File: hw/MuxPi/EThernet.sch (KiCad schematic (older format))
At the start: 36 parts, among them J3 TJACKCFL8P8CSR06M1, U11 93AA56AT-I/OT, U12 LAN9500A-ABZJ, Y3 25.00M-SMDHC49S

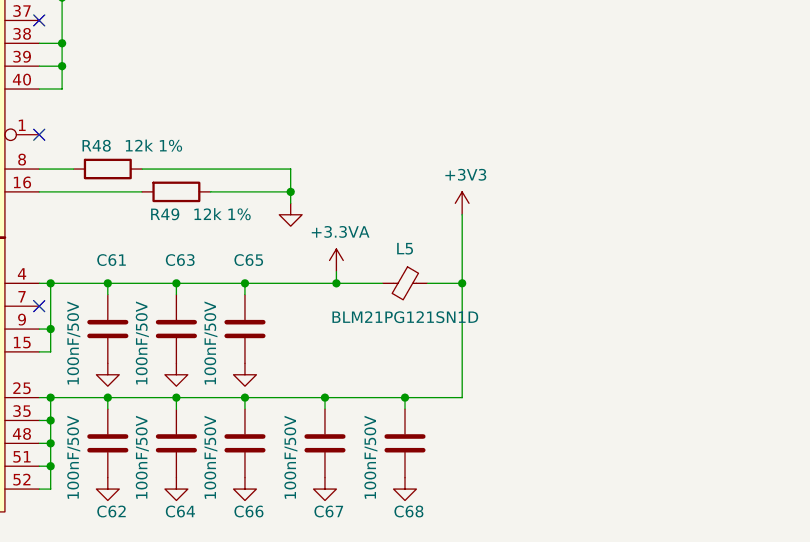
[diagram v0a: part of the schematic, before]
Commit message: Add detailed info to MuxPi electronic components
The additional information includes manufacturer names and
manufacturer symbols for all components except ceramic capacitors
and resistors. It allows to create BOM (Bill Of Materials) with
actual product names.

Change-Id: Id1c518bba60322d4b8b132ad14261806070abc27
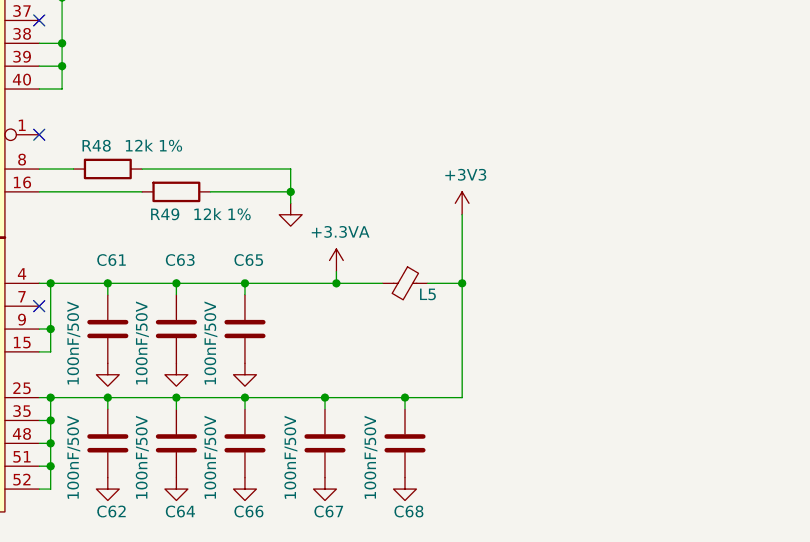
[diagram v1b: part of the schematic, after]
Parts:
- J3: Manufacturer (none) -> CZT; Symbol (none) -> JDFD10141104 TS-10014-11(6U)
- L3, L4, L5: Manufacturer (none) -> MURATA; Symbol (none) -> BLM21PG121SN1D
- U11: Manufacturer (none) -> MICROCHIP; Symbol (none) -> 93AA56AT-I/OT
- U12: Manufacturer (none) -> MICROCHIP; Symbol (none) -> LAN9500A-ABZJ
- Y3: Manufacturer (none) -> YIC; Symbol (none) -> 25.00M-SMDHC49S
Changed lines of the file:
@@
 F 3 "http://www.farnell.com/datasheets/1907741.pdf?_ga=1.91944537.291132730.1474618953" H 6150 2250 50  0001 C CNN
 F 4 "http://pl.farnell.com/microchip/lan9500a-abzj/ic-usb2-0-10-100-enet-cntrl-56vqfn/dp/2292585" H 4200 2500 60  0001 C CNN "Shop link"
+F 5 "LAN9500A-ABZJ" H 4200 2500 50  0001 C CNN "Symbol"
+F 6 "MICROCHIP" H 4200 2500 50  0001 C CNN "Manufacturer"
 	1    4200 2500
 	1    0    0    -1
@@
 F 3 "http://www.farnell.com/datasheets/1907741.pdf?_ga=1.91944537.291132730.1474618953" H 5800 6000 50  0001 C CNN
 F 4 "http://pl.farnell.com/microchip/lan9500a-abzj/ic-usb2-0-10-100-enet-cntrl-56vqfn/dp/2292585" H 3850 6250 60  0001 C CNN "Shop link"
+F 5 "MICROCHIP" H 3850 6250 50  0001 C CNN "Manufacturer"
+F 6 "LAN9500A-ABZJ" H 3850 6250 50  0001 C CNN "Symbol"
 	2    3850 6250
 	1    0    0    -1
@@
 $EndComp
 $Comp
-L MuxPi:Ferrite_Bead_Small L5
-U 1 1 585E1E42
-P 6250 6450
-F 0 "L5" V 6100 6450 50  0000 C CNN
-F 1 "BLM21PG121SN1D" V 6400 6450 50  0000 C CNN
-F 2 "Resistors_SMD:R_0805_HandSoldering" H 6350 6359 50  0001 L CNN
-F 3 "http://www.tme.eu/pl/Document/6052c7f9d4f1672121538e0d10f79ff8/blm21pg300sn1d.pdf" H 6350 6359 50  0001 L CNN
-F 4 "http://www.tme.eu/pl/details/blm21pg121sn1d/ferryty-koraliki/murata/" H 6250 6450 60  0001 C CNN "Shop link"
-	1    6250 6450
-	0    1    1    0
-$EndComp
-$Comp
 L MuxPi:GND #PWR0171
 U 1 1 585E2006
@@
 $EndComp
 $Comp
-L MuxPi:Ferrite_Bead_Small L4
-U 1 1 585E3856
-P 2450 6550
-F 0 "L4" V 2500 6650 50  0000 C CNN
-F 1 "BLM21PG121SN1D" V 2304 6550 50  0001 C CNN
-F 2 "Resistors_SMD:R_0805_HandSoldering" H 2550 6459 50  0001 L CNN
-F 3 "http://www.tme.eu/pl/Document/6052c7f9d4f1672121538e0d10f79ff8/blm21pg300sn1d.pdf" H 2550 6459 50  0001 L CNN
-F 4 "http://www.tme.eu/pl/details/blm21pg121sn1d/ferryty-koraliki/murata/" H 2450 6550 60  0001 C CNN "Shop link"
-	1    2450 6550
-	0    1    1    0
-$EndComp
-$Comp
 L MuxPi:GND #PWR0165
 U 1 1 585E3BDA
@@
 F 3 "http://www.tme.eu/pl/Document/6052c7f9d4f1672121538e0d10f79ff8/blm21pg300sn1d.pdf" H 2100 6359 50  0001 L CNN
 F 4 "http://www.tme.eu/pl/details/blm21pg121sn1d/ferryty-koraliki/murata/" H 2000 6450 60  0001 C CNN "Shop link"
+F 5 "MURATA" V 2000 6450 50  0001 C CNN "Manufacturer"
+F 6 "BLM21PG121SN1D" V 2000 6450 50  0001 C CNN "Symbol"
 	1    2000 6450
 	0    1    1    0
@@
 F 3 "http://www.tme.eu/pl/Document/6527d4ac6cd20f858e4312ccc80ef7ce/YIC-49US_49SMT-quartz_crystal.pdf" H 1900 6100 50  0001 C CNN
 F 4 "http://www.tme.eu/pl/details/25.00m-smdhc49s/rezonatory-kwarcowe-smd/yic/" V 1900 6100 60  0001 C CNN "Shop link"
+F 5 "YIC" V 1900 6100 50  0001 C CNN "Manufacturer"
+F 6 "25.00M-SMDHC49S" V 1900 6100 50  0001 C CNN "Symbol"
 	1    1900 6100
 	0    1    1    0
@@
 F 3 "http://www.farnell.com/datasheets/1669363.pdf?_ga=1.23852537.291132730.1474618953" H 2350 2600 50  0001 C CNN
 F 4 "http://pl.farnell.com/microchip/93aa56at-i-ot/serial-eeprom-2kbit-2mhz-sot-23/dp/1331419" H 2450 2600 60  0001 C CNN "Shop link"
+F 5 "MICROCHIP" H 2450 2600 50  0001 C CNN "Manufacturer"
+F 6 "93AA56AT-I/OT" H 2450 2600 50  0001 C CNN "Symbol"
 	1    2450 2600
 	-1   0    0    -1
@@
 F 3 "https://www.maritex.com.pl/product/attachment/41725/TJACKCFL8P8CSB06-MAG1_new.pdf" H 9050 2523 50  0001 C CNN
 F 4 "https://www.maritex.com.pl/zlacza/zlacza_rj_modularne/zlacza_rj_1_x_port/zlacza_rj_gniazda_modularne_ekranowane_diody_led_transformator_separujacy/tjackcfl8p8csr06m1.html" H 9300 1900 60  0001 C CNN "Shop link"
+F 5 "CZT" H 9300 1900 50  0001 C CNN "Manufacturer"
+F 6 "JDFD10141104 TS-10014-11(6U)" H 9300 1900 50  0001 C CNN "Symbol"
 	1    9300 1900
 	1    0    0    -1
@@
 Wire Wire Line
 	9950 2650 10100 2650
+$Comp
+L MuxPi:Ferrite_Bead_Small L4
+U 1 1 5A8E75C9
+P 2450 6550
+F 0 "L4" V 2500 6650 50  0000 C CNN
+F 1 "BLM21PG121SN1D" V 2304 6550 50  0001 C CNN
+F 2 "Resistors_SMD:R_0805_HandSoldering" H 2550 6459 50  0001 L CNN
+F 3 "http://www.tme.eu/pl/Document/6052c7f9d4f1672121538e0d10f79ff8/blm21pg300sn1d.pdf" H 2550 6459 50  0001 L CNN
+F 4 "http://www.tme.eu/pl/details/blm21pg121sn1d/ferryty-koraliki/murata/" H 2450 6550 60  0001 C CNN "Shop link"
+F 5 "MURATA" V 2450 6550 50  0001 C CNN "Manufacturer"
+F 6 "BLM21PG121SN1D" V 2450 6550 50  0001 C CNN "Symbol"
+	1    2450 6550
+	0    1    1    0
+$EndComp
+$Comp
+L MuxPi:Ferrite_Bead_Small L5
+U 1 1 5A8E7FF7
+P 6250 6450
+F 0 "L5" V 6300 6550 50  0000 C CNN
+F 1 "BLM21PG121SN1D" V 6104 6450 50  0001 C CNN
+F 2 "Resistors_SMD:R_0805_HandSoldering" H 6350 6359 50  0001 L CNN
+F 3 "http://www.tme.eu/pl/Document/6052c7f9d4f1672121538e0d10f79ff8/blm21pg300sn1d.pdf" H 6350 6359 50  0001 L CNN
+F 4 "http://www.tme.eu/pl/details/blm21pg121sn1d/ferryty-koraliki/murata/" H 6250 6450 60  0001 C CNN "Shop link"
+F 5 "MURATA" V 6250 6450 50  0001 C CNN "Manufacturer"
+F 6 "BLM21PG121SN1D" V 6250 6450 50  0001 C CNN "Symbol"
+	1    6250 6450
+	0    1    1    0
+$EndComp
 $EndSCHEMATC

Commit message: Update hardware design to version 1.3
Change-Id: I17b3f32943a6fd048f05d1b0d8676607dc54b976
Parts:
- C58, C59: footprint Capacitors_SMD:C_0402 -> Capacitors_SMD:C_0805
- L3, L4, L5: footprint Resistors_SMD:R_0805_HandSoldering -> Resistors_SMD:R_0805
- R48, R49: footprint Resistors_SMD:R_0402 -> Resistors_SMD:R_0805
- R56: value 330R -> 10K; Shop link http://www.tme.eu/pl/details/rc0805jr-07330r/rezystory-smd-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 -> (none)
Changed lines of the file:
@@
 Sheet 11 12
 Title "MuxPi"
-Date "2018-04-20"
-Rev "1.2"
+Date "2018-08-14"
+Rev "1.3"
 Comp "SRPOL"
 Comment1 "Author: Adam Malinowski <a.malinowsk2@partner.samsung.com>"
-Comment2 "Copyright (c) 2016 - 2018 Samsung Electronics Co., Ltd All Rights Reserved"
+Comment2 "Copyright (c) 2016 -2018 Samsung Electronics Co., Ltd All Rights Reserved"
 Comment3 ""
 Comment4 ""
@@
 F 0 "L3" V 2050 6550 50  0000 C CNN
 F 1 "BLM21PG121SN1D" V 1854 6450 50  0001 C CNN
-F 2 "Resistors_SMD:R_0805_HandSoldering" H 2100 6359 50  0001 L CNN
+F 2 "Resistors_SMD:R_0805" H 2100 6359 50  0001 L CNN
 F 3 "http://www.tme.eu/pl/Document/6052c7f9d4f1672121538e0d10f79ff8/blm21pg300sn1d.pdf" H 2100 6359 50  0001 L CNN
 F 4 "http://www.tme.eu/pl/details/blm21pg121sn1d/ferryty-koraliki/murata/" H 2000 6450 60  0001 C CNN "Shop link"
@@
 F 0 "C59" H 2350 5550 50  0000 L CNN
 F 1 "100nF/50V" H 2300 5050 50  0000 L CNN
-F 2 "Capacitors_SMD:C_0402" H 2538 5250 50  0001 C CNN
+F 2 "Capacitors_SMD:C_0805" H 2538 5250 50  0001 C CNN
 F 3 "http://www.tme.eu/pl/Document/4a42202b32dab16128fe107dd69598cc/samsung-chip-cap.pdf" H 2500 5400 50  0001 C CNN
 F 4 "http://www.tme.eu/pl/details/cl21b331kbannnc/kondensatory-mlcc-smd-0805/samsung/" H 2500 5400 60  0001 C CNN "Shop link"
@@
 F 0 "C58" H 2300 7200 50  0000 L CNN
 F 1 "100nF/50V" H 2050 6650 50  0000 L CNN
-F 2 "Capacitors_SMD:C_0402" H 2288 6900 50  0001 C CNN
+F 2 "Capacitors_SMD:C_0805" H 2288 6900 50  0001 C CNN
 F 3 "http://www.tme.eu/pl/Document/4a42202b32dab16128fe107dd69598cc/samsung-chip-cap.pdf" H 2250 7050 50  0001 C CNN
 F 4 "http://www.tme.eu/pl/details/cl21b331kbannnc/kondensatory-mlcc-smd-0805/samsung/" H 2250 7050 60  0001 C CNN "Shop link"
@@
 F 0 "R48" V 4850 5900 50  0000 C CNN
 F 1 "12k 1%" V 4850 6150 50  0000 C CNN
-F 2 "Resistors_SMD:R_0402" V 4880 5950 30  0001 C CNN
+F 2 "Resistors_SMD:R_0805" V 4880 5950 30  0001 C CNN
 F 3 "http://www.tme.eu/pl/Document/7b8fed8c112f8a94930279c22c957f7f/rc0805yageo.pdf" H 4950 5950 30  0001 C CNN
 F 4 "http://www.tme.eu/pl/details/rc0805fr-0712k/rezystory-smd-0805/yageo/rc0805fr-0712kl/" V 4950 5950 60  0001 C CNN "Shop link"
@@
 F 0 "R49" V 5350 6000 50  0000 C CNN
 F 1 "12k 1%" V 5350 6250 50  0000 C CNN
-F 2 "Resistors_SMD:R_0402" V 5180 6050 30  0001 C CNN
+F 2 "Resistors_SMD:R_0805" V 5180 6050 30  0001 C CNN
 F 3 "http://www.tme.eu/pl/Document/7b8fed8c112f8a94930279c22c957f7f/rc0805yageo.pdf" H 5250 6050 30  0001 C CNN
 F 4 "http://www.tme.eu/pl/details/rc0805fr-0712k/rezystory-smd-0805/yageo/rc0805fr-0712kl/" V 5250 6050 60  0001 C CNN "Shop link"
@@
 P 9800 2850
 F 0 "R56" H 9600 2900 50  0000 L CNN
-F 1 "330R" H 9500 2800 50  0000 L CNN
+F 1 "10K" H 9500 2800 50  0000 L CNN
 F 2 "Resistors_SMD:R_0805" V 9730 2850 50  0001 C CNN
 F 3 "http://www.tme.eu/pl/Document/7b8fed8c112f8a94930279c22c957f7f/rc0805yageo.pdf" H 9800 2850 50  0001 C CNN
-F 4 "http://www.tme.eu/pl/details/rc0805jr-07330r/rezystory-smd-0805/yageo/rc0805jr-07330rl/" V 9800 2850 60  0001 C CNN "Shop link"
 	1    9800 2850
 	1    0    0    -1
@@
 F 0 "L4" V 2500 6650 50  0000 C CNN
 F 1 "BLM21PG121SN1D" V 2304 6550 50  0001 C CNN
-F 2 "Resistors_SMD:R_0805_HandSoldering" H 2550 6459 50  0001 L CNN
+F 2 "Resistors_SMD:R_0805" H 2550 6459 50  0001 L CNN
 F 3 "http://www.tme.eu/pl/Document/6052c7f9d4f1672121538e0d10f79ff8/blm21pg300sn1d.pdf" H 2550 6459 50  0001 L CNN
 F 4 "http://www.tme.eu/pl/details/blm21pg121sn1d/ferryty-koraliki/murata/" H 2450 6550 60  0001 C CNN "Shop link"
@@
 F 0 "L5" V 6300 6550 50  0000 C CNN
 F 1 "BLM21PG121SN1D" V 6104 6450 50  0001 C CNN
-F 2 "Resistors_SMD:R_0805_HandSoldering" H 6350 6359 50  0001 L CNN
+F 2 "Resistors_SMD:R_0805" H 6350 6359 50  0001 L CNN
 F 3 "http://www.tme.eu/pl/Document/6052c7f9d4f1672121538e0d10f79ff8/blm21pg300sn1d.pdf" H 6350 6359 50  0001 L CNN
 F 4 "http://www.tme.eu/pl/details/blm21pg121sn1d/ferryty-koraliki/murata/" H 6250 6450 60  0001 C CNN "Shop link"

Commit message: Update  hardware design to version 1.4
Change-Id: I72a4381d8bec5616bc1cfe04dc8a5407141c77d5
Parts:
- removed Y3: 25.00M-SMDHC49S, Crystals:Q_49U3HMS, symbol MuxPi:Crystal
- added Y3: 25.00M-CFPX218, Crystal:Crystal_SMD_2520-4Pin_2.5x2.0mm, symbol Device:Crystal_GND24
- C54: value 30pF/50V -> 33pF/50V; Shop link http://www.tme.eu/pl/details/cl21c330jbannnd/kondensatory-m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 -> https://pl.farnell.com/walsin/0805n330j500ct/cap-33pf-50v-5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
- C55: value 30pF/50V -> 33pF/50V; footprint Capacitors_SMD:C_0805 -> MuxPi:C_0805; Shop link http://www.tme.eu/pl/details/cl21c330jbannnd/kondensatory-m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 -> https://pl.farnell.com/walsin/0805n330j500ct/cap-33pf-50v-5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
- R53, R54: value 330R -> 560R; Shop link http://www.tme.eu/pl/details/rc0805jr-07330r/rezystory-smd-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 -> https://www.tme.eu/pl/details/rc0805jr-07560r/rezystory-smd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
- U11: Assembly (none) -> DNP
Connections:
- net GND: now also Y3.2, Y3.4
- net at C55.1, U12.19 (XO): now also Y3.3
- net at C54.1, U12.18 (XI): now also Y3.1
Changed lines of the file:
@@
 EESchema Schematic File Version 4
 LIBS:MuxPi-cache
-EELAYER 26 0
+EELAYER 29 0
 EELAYER END
 $Descr A4 11693 8268
@@
 Sheet 11 12
 Title "MuxPi"
-Date "2018-08-14"
-Rev "1.3"
+Date "2018-11-16"
+Rev "1.4"
 Comp "SRPOL"
 Comment1 "Author: Adam Malinowski <a.malinowsk2@partner.samsung.com>"
@@
 $EndComp
 $Comp
-L MuxPi:Crystal Y3
-U 1 1 585EE4AB
-P 1900 6100
-F 0 "Y3" V 1750 6000 50  0000 C CNN
-F 1 "25.00M-SMDHC49S" V 1600 6100 50  0000 C CNN
-F 2 "Crystals:Q_49U3HMS" H 1900 6100 50  0001 C CNN
-F 3 "http://www.tme.eu/pl/Document/6527d4ac6cd20f858e4312ccc80ef7ce/YIC-49US_49SMT-quartz_crystal.pdf" H 1900 6100 50  0001 C CNN
-F 4 "http://www.tme.eu/pl/details/25.00m-smdhc49s/rezonatory-kwarcowe-smd/yic/" V 1900 6100 60  0001 C CNN "Shop link"
-F 5 "YIC" V 1900 6100 50  0001 C CNN "Manufacturer"
-F 6 "25.00M-SMDHC49S" V 1900 6100 50  0001 C CNN "Symbol"
-	1    1900 6100
-	0    1    1    0
-$EndComp
-$Comp
 L MuxPi:GND #PWR0156
 U 1 1 585EE4B2
@@
 P 1450 5850
 F 0 "C54" V 1300 5800 50  0000 L CNN
-F 1 "30pF/50V" V 1600 5700 50  0000 L CNN
+F 1 "33pF/50V" V 1600 5700 50  0000 L CNN
 F 2 "Capacitors_SMD:C_0805" H 1488 5700 30  0001 C CNN
-F 3 "http://www.tme.eu/pl/Document/4a42202b32dab16128fe107dd69598cc/samsung-chip-cap.pdf" H 1450 5850 60  0001 C CNN
-F 4 "http://www.tme.eu/pl/details/cl21c330jbannnd/kondensatory-mlcc-smd-0805/samsung/" V 1450 5850 60  0001 C CNN "Shop link"
+F 3 "http://www.farnell.com/datasheets/2340522.pdf" H 1450 5850 60  0001 C CNN
+F 4 "https://pl.farnell.com/walsin/0805n330j500ct/cap-33pf-50v-5-c0g-np0-0805-reel/dp/2495530" V 1450 5850 60  0001 C CNN "Shop link"
 	1    1450 5850
 	0    1    1    0
@@
 F 5 "MICROCHIP" H 2450 2600 50  0001 C CNN "Manufacturer"
 F 6 "93AA56AT-I/OT" H 2450 2600 50  0001 C CNN "Symbol"
+F 7 "DNP" H 2450 2300 50  0000 C CIB "Assembly"
 	1    2450 2600
 	-1   0    0    -1
@@
 	2200 6150 2200 6350
 Wire Wire Line
-	1200 5850 1200 6350
+	1200 5850 1200 6100
 Connection ~ 1200 6350
 Wire Wire Line
@@
 P 7100 2100
 F 0 "R53" V 7000 2050 50  0000 L CNN
-F 1 "330R" V 7050 2250 50  0000 L CNN
+F 1 "560R" V 7050 2250 50  0000 L CNN
 F 2 "Resistors_SMD:R_0805" V 7030 2100 50  0001 C CNN
 F 3 "http://www.tme.eu/pl/Document/7b8fed8c112f8a94930279c22c957f7f/rc0805yageo.pdf" H 7100 2100 50  0001 C CNN
-F 4 "http://www.tme.eu/pl/details/rc0805jr-07330r/rezystory-smd-0805/yageo/rc0805jr-07330rl/" V 7100 2100 60  0001 C CNN "Shop link"
+F 4 "https://www.tme.eu/pl/details/rc0805jr-07560r/rezystory-smd-0805/yageo/rc0805jr-07560rl/" V 7100 2100 60  0001 C CNN "Shop link"
 	1    7100 2100
 	0    1    1    0
@@
 P 7100 2300
 F 0 "R54" V 7250 2250 50  0000 L CNN
-F 1 "330R" V 7050 2450 50  0000 L CNN
+F 1 "560R" V 7050 2450 50  0000 L CNN
 F 2 "Resistors_SMD:R_0805" V 7030 2300 50  0001 C CNN
 F 3 "http://www.tme.eu/pl/Document/7b8fed8c112f8a94930279c22c957f7f/rc0805yageo.pdf" H 7100 2300 50  0001 C CNN
-F 4 "http://www.tme.eu/pl/details/rc0805jr-07330r/rezystory-smd-0805/yageo/rc0805jr-07330rl/" V 7100 2300 60  0001 C CNN "Shop link"
+F 4 "https://www.tme.eu/pl/details/rc0805jr-07560r/rezystory-smd-0805/yageo/rc0805jr-07560rl/" V 7100 2300 60  0001 C CNN "Shop link"
 	1    7100 2300
 	0    1    1    0
@@
 	1    7150 1150
 	1    0    0    -1
-$EndComp
-$Comp
-L MuxPi:C C55
-U 1 1 5853EA53
-P 1450 6350
-F 0 "C55" V 1300 6300 50  0000 L CNN
-F 1 "30pF/50V" V 1600 6200 50  0000 L CNN
-F 2 "Capacitors_SMD:C_0805" H 1488 6200 30  0001 C CNN
-F 3 "http://www.tme.eu/pl/Document/4a42202b32dab16128fe107dd69598cc/samsung-chip-cap.pdf" H 1450 6350 60  0001 C CNN
-F 4 "http://www.tme.eu/pl/details/cl21c330jbannnd/kondensatory-mlcc-smd-0805/samsung/" V 1450 6350 60  0001 C CNN "Shop link"
-	1    1450 6350
-	0    1    1    0
 $EndComp
 Text Label 5550 1450 0    60   ~ 0
@@
 	0    1    1    0
 $EndComp
+$Comp
+L MuxPi:C C55
+U 1 1 5BEDDA2A
+P 1450 6350
+F 0 "C55" V 1300 6300 50  0000 L CNN
+F 1 "33pF/50V" V 1600 6200 50  0000 L CNN
+F 2 "MuxPi:C_0805" H 1488 6200 30  0001 C CNN
+F 3 "http://www.farnell.com/datasheets/2340522.pdf" H 1450 6350 60  0001 C CNN
+F 4 "https://pl.farnell.com/walsin/0805n330j500ct/cap-33pf-50v-5-c0g-np0-0805-reel/dp/2495530" V 1450 6350 60  0001 C CNN "Shop link"
+	1    1450 6350
+	0    1    1    0
+$EndComp
+$Comp
+L Device:Crystal_GND24 Y?
+U 1 1 5BF5EFA3
+P 1900 6100
+AR Path="/584D6534/5BF5EFA3" Ref="Y?"  Part="1"
+AR Path="/584BEF7D/5BF5EFA3" Ref="Y3"  Part="1"
+F 0 "Y3" V 1700 6150 50  0000 L CNN
+F 1 "25.00M-CFPX218" V 1300 5600 50  0000 L CNN
+F 2 "Crystal:Crystal_SMD_2520-4Pin_2.5x2.0mm" H 1900 6100 50  0001 C CNN
+F 3 "http://www.tme.eu/pl/Document/43d4b8b2418f10b1847f5f6593a9a63f/cfpx-218.pdf" H 1900 6100 50  0001 C CNN
+F 4 "https://www.tme.eu/pl/details/25.00m-cfpx218/rezonatory-kwarcowe-smd/iqd-frequency-products/lfxtal053108bulk/" H 1900 6100 50  0001 C CNN "Shop link"
+F 5 "IQD FREQUENCY PRODUCTS" H 1900 6100 50  0001 C CNN "Manufacturer"
+F 6 "LFXTAL053108BULK" H 1900 6100 50  0001 C CNN "Symbol"
+	1    1900 6100
+	0    1    1    0
+$EndComp
+$Comp
+L MuxPi:GND #PWR0203
+U 1 1 5BF680BA
+P 2350 6250
+F 0 "#PWR0203" H 2350 6000 50  0001 C CNN
+F 1 "GND" H 2355 6077 50  0001 C CNN
+F 2 "" H 2350 6250 50  0000 C CNN
+F 3 "" H 2350 6250 50  0000 C CNN
+	1    2350 6250
+	1    0    0    -1
+$EndComp
+Wire Wire Line
+	2350 6250 2350 6100
+Wire Wire Line
+	2350 6100 2100 6100
+Wire Wire Line
+	1700 6100 1200 6100
+Wire Wire Line
+	1200 6100 1200 6350
+Connection ~ 1200 6100
 $EndSCHEMATC
